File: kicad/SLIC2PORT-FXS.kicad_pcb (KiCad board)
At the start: 2 copper layers, 120 x 90 mm, 160 parts, among them J1 USB-C_PWR, J2 DC5V_IN, J5 EXPANSION, J6 UART_DBG, K1 G5V-2_DC5, K2 G5V-2_DC5, Q1 AO3401A, Q2 2N7002, Q3 2N7002, Q4 2N7002, Q5 2N7002, Q6 2N7002, SW1 RST, SW2 BOOT, U1 M5StampS3/S3A, U106 1N4007, U2 74HCT244, U45 1N4007, U49 1N4007, U55 P3100SC, U56 1N4007, U57 1N4007, U58 1N4007, U59 1N4007, U60 BZT03C82, U64 BK2125HS601-T, U79 1N4007, U82 P3100SC, U83 1N4007, U84 1N4007, U85 1N4007, U86 1N4007, U87 BZT03C82, U91 BK2125HS601-T

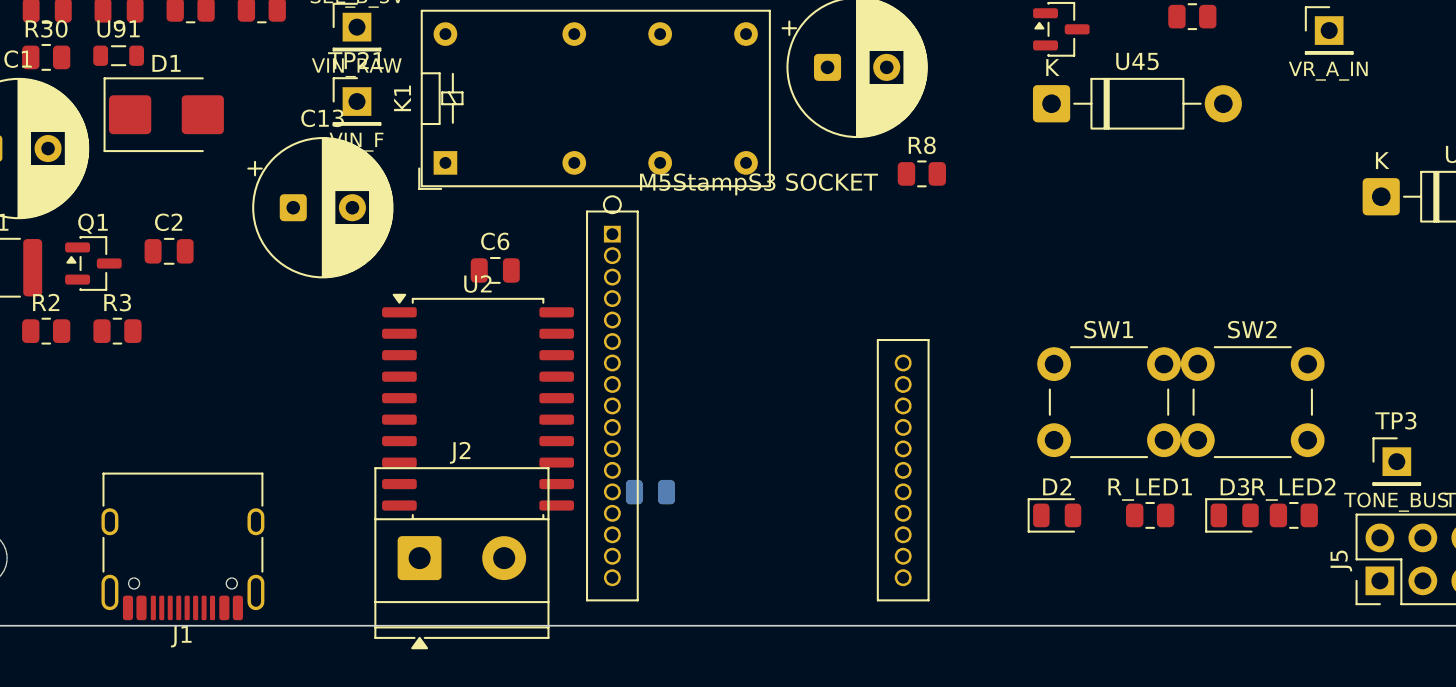
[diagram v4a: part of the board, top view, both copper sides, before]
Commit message: Fix ring-test redial, pin the ESP32 core, and separate shorted switches
Single-port ring test treated a 10 ms off-hook as both ends on-hook and
then originated a call. PlatformIO is pinned to espressif32 8.0.0 so
ledcAttach builds. SW1/SW2 no longer short EN to GPIO0, and the USB-C
pads clear the board edge.

Co-authored-by: GOROman <GOROman@users.noreply.github.com>
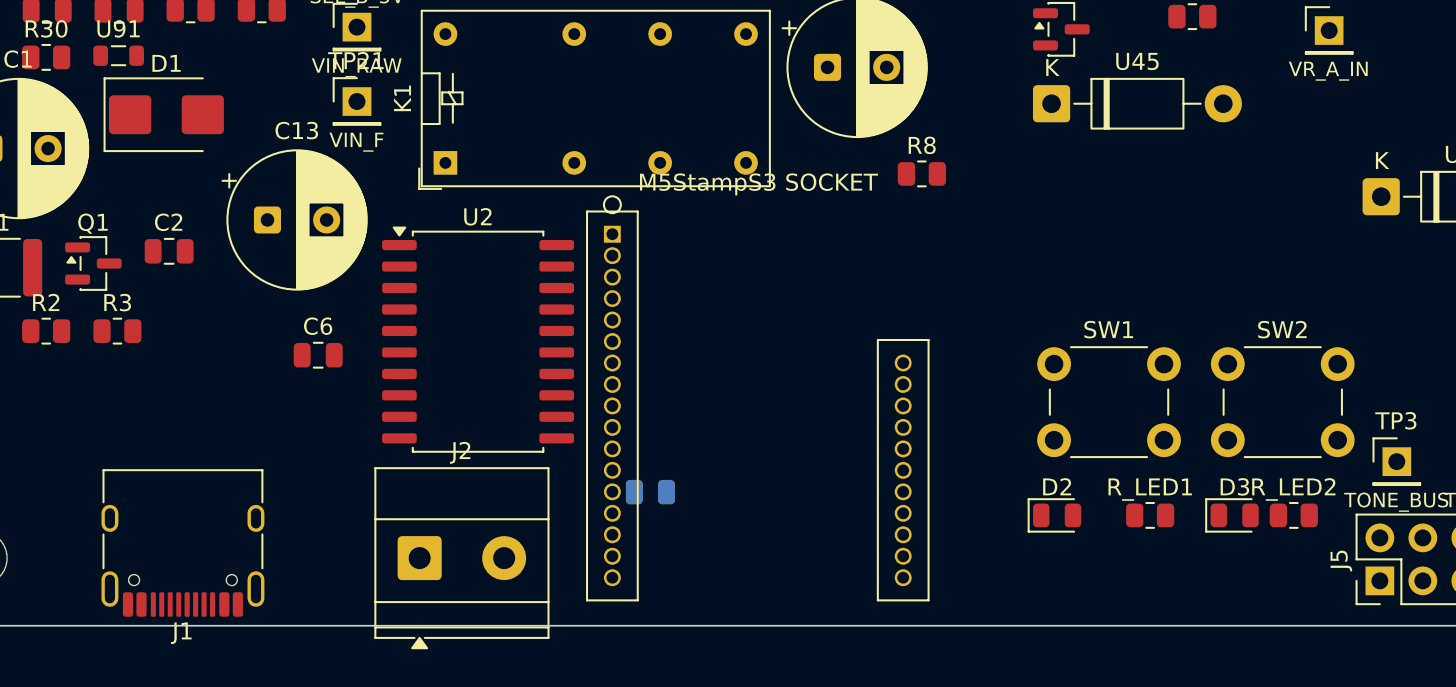
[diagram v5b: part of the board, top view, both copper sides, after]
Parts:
- moved C6 11.6 mm to (24.0, 74.0)
- moved U2 3.97 mm to (33.5, 73.2)
- moved SW2 1.77 mm to (77.8, 74.5)
- moved C13 1.69 mm to (21.0, 66.0)
- moved J1 0.20 mm to (16.0, 84.7)
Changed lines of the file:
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@@
 	(footprint "SW_PUSH_6mm"
 		(layer "F.Cu")
-		(at 76.025 74.525)
+		(at 77.8 74.525)
 		(descr "Generic 6mm SW tactile push button")
 		(tags "tact sw push 6mm")
@@
 	(footprint "SOIC-20W_7.5x12.8mm_P1.27mm"
 		(layer "F.Cu")
-		(at 33.455 77.175)
+		(at 33.455 73.2)
 		(descr "SOIC, 20 Pin (JEDEC MS-013AC, https://www.analog.com/media/en/package-pcb-resources/package/233848rw_20.pdf)")
 		(tags "SOIC SO")
@@
 	(footprint "USB_C_Receptacle_HRO_TYPE-C-31-M-12"
 		(layer "F.Cu")
-		(at 16 84.9 180)
+		(at 16 84.7 180)
 		(descr "USB Type-C receptacle for USB 2.0 and PD, http://www.krhro.com/uploads/soft/180320/1-1P320120243.pdf")
 		(tags "usb usb-c 2.0 pd")
@@
 	(footprint "C_0805_2012Metric"
 		(layer "F.Cu")
-		(at 34.475 68.985)
+		(at 24 74)
 		(descr "Capacitor SMD 0805 (2012 Metric), square (rectangular) end terminal, IPC-7351 nominal, (Body size source: IPC-SM-782 page 76, https://www.pcb-3d.com/wordpress/wp-content/uploads/ipc-sm-782a_amendment_1_and_2.pdf, https://docs.google.com/spreadsheets/d/1BsfQQcO9C6DZCsRaXUlFlo91Tg2WpOkGARC1WS5S8t0/edit?usp=sharing)")
 		(tags "capacitor")
@@
 	(footprint "CP_Radial_D8.0mm_P3.50mm"
 		(layer "F.Cu")
-		(at 22.525 65.275)
+		(at 21 66)
 		(descr "CP, Radial series, Radial, pin pitch=3.50mm, diameter=8mm, height=12mm, Electrolytic Capacitor")
 		(tags "CP Radial series Radial pin pitch 3.50mm diameter 8mm height 12mm Electrolytic Capacitor")
